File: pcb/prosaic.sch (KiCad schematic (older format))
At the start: 16 parts, among them J1 USB_C_Receptacle, SW1 SW_PUSH, U1 ATMEGA32U4, X1 XTAL_GND

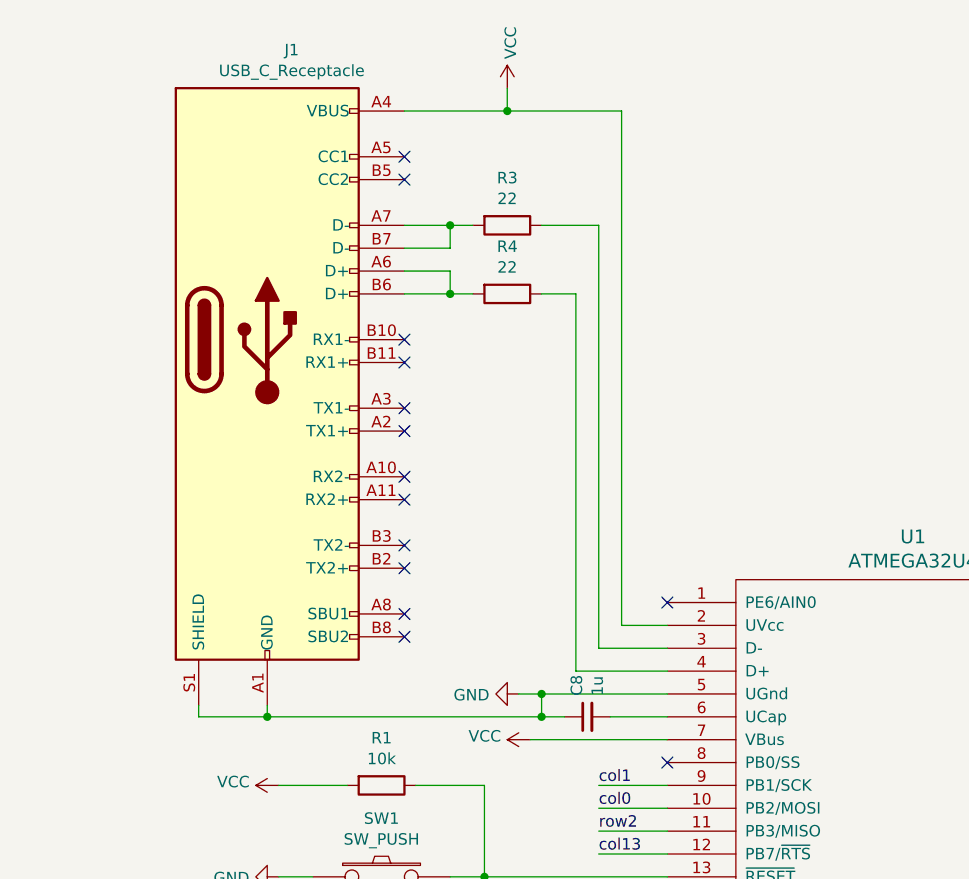
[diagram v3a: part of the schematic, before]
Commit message: Made trace change around crystal; updated case cad
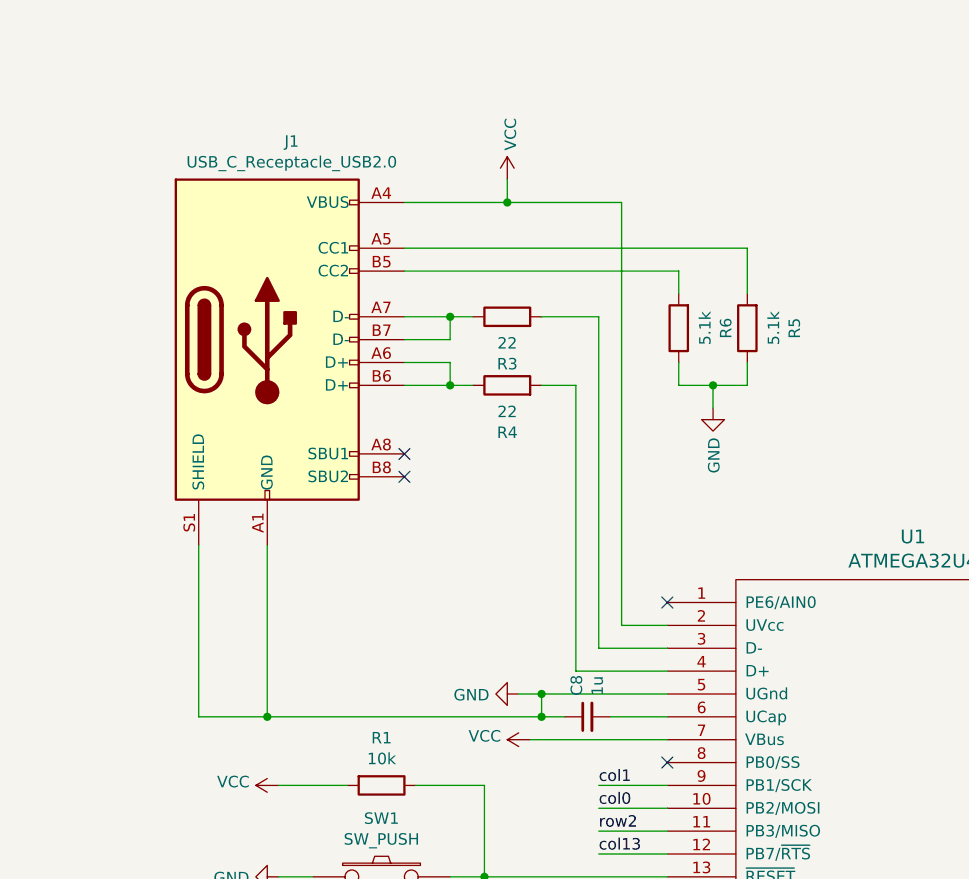
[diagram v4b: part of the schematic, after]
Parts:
- removed J1: USB_C_Receptacle, Connector_USB:USB_C_Receptacle_Amphenol_12401610E4-2A, symbol Connector:USB_C_Receptacle
- added J1: USB_C_Receptacle_USB2.0, Connector_USB:USB_C_Receptacle_GCT_USB4085, symbol Connector:USB_C_Receptacle_USB2.0
- added R5, R6: 5.1k, Resistor_SMD:R_0805_2012Metric_Pad1.15x1.40mm_HandSolder, symbol Device:R
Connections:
- net GND: now also J1.A1 (GND), J1.A12 (GND), J1.B1 (GND), J1.B12 (GND), J1.S1 (SHIELD), R5.1, R6.1
- net VCC: now also J1.A4 (VBUS), J1.A9 (VBUS), J1.B4 (VBUS), J1.B9 (VBUS)
- net at R4.1: now also J1.A6 (D+), J1.B6 (D+); no longer U1.4 (D+)
- net at R4.2: now also U1.4 (D+)
- net at R3.1: now also J1.A7 (D-), J1.B7 (D-); no longer U1.3 (D-)
- net at R3.2: now also U1.3 (D-)
- new net: J1.B5 (CC2), R6.2
- new net: J1.A5 (CC1), R5.2
- no-connect marks 16 -> 6
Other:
- moved on the sheet: R3, R4
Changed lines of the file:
@@
 Sheet 1 2
 Title "Prosaic"
-Date "2020-07-28"
-Rev "A"
+Date "2020-08-02"
+Rev "A.1"
 Comp ""
 Comment1 "by SiriusSam"
@@
 	6250 3850 6650 3850
 Wire Wire Line
-	6100 2200 6250 2200
+	6100 2600 6250 2600
 Wire Wire Line
 	6350 3750 6650 3750
 Wire Wire Line
-	6350 1900 6350 3750
-Wire Wire Line
-	5700 2100 5700 2200
-Wire Wire Line
-	5700 2000 5700 1900
+	5700 2500 5700 2600
+Wire Wire Line
+	5700 2400 5700 2300
 $Comp
 L Device:R R4
 U 1 1 5F1AE097
-P 5950 2200
-F 0 "R4" V 5743 2200 50  0000 C CNN
-F 1 "22" V 5834 2200 50  0000 C CNN
-F 2 "Resistor_SMD:R_0805_2012Metric_Pad1.15x1.40mm_HandSolder" V 5880 2200 50  0001 C CNN
-F 3 "~" H 5950 2200 50  0001 C CNN
-	1    5950 2200
-	0    1    1    0
+P 5950 2600
+F 0 "R4" V 5743 2600 50  0000 C CNN
+F 1 "22" V 5834 2600 50  0000 C CNN
+F 2 "Resistor_SMD:R_0805_2012Metric_Pad1.15x1.40mm_HandSolder" V 5880 2600 50  0001 C CNN
+F 3 "~" H 5950 2600 50  0001 C CNN
+	1    5950 2600
+	0    -1   -1   0
 $EndComp
 $Comp
 L Device:R R3
 U 1 1 5F1AE09D
-P 5950 1900
-F 0 "R3" V 5743 1900 50  0000 C CNN
-F 1 "22" V 5834 1900 50  0000 C CNN
-F 2 "Resistor_SMD:R_0805_2012Metric_Pad1.15x1.40mm_HandSolder" V 5880 1900 50  0001 C CNN
-F 3 "~" H 5950 1900 50  0001 C CNN
-	1    5950 1900
-	0    1    1    0
-$EndComp
-Connection ~ 5950 1400
-Wire Wire Line
-	6450 1400 5950 1400
-Wire Wire Line
-	6450 3650 6450 1400
+P 5950 2300
+F 0 "R3" V 5743 2300 50  0000 C CNN
+F 1 "22" V 5834 2300 50  0000 C CNN
+F 2 "Resistor_SMD:R_0805_2012Metric_Pad1.15x1.40mm_HandSolder" V 5880 2300 50  0001 C CNN
+F 3 "~" H 5950 2300 50  0001 C CNN
+	1    5950 2300
+	0    -1   -1   0
+$EndComp
+Connection ~ 5950 1800
+Wire Wire Line
+	6450 1800 5950 1800
 Wire Wire Line
 	6650 3650 6450 3650
 Wire Wire Line
-	5950 1300 5950 1400
+	5950 1700 5950 1800
 $Comp
 L power:VCC #PWR0110
 U 1 1 5F1AE0A9
-P 5950 1300
-F 0 "#PWR0110" H 5950 1150 50  0001 C CNN
-F 1 "VCC" V 5965 1427 50  0000 L CNN
-F 2 "" H 5950 1300 50  0001 C CNN
-F 3 "" H 5950 1300 50  0001 C CNN
-	1    5950 1300
+P 5950 1700
+F 0 "#PWR0110" H 5950 1550 50  0001 C CNN
+F 1 "VCC" V 5965 1827 50  0000 L CNN
+F 2 "" H 5950 1700 50  0001 C CNN
+F 3 "" H 5950 1700 50  0001 C CNN
+	1    5950 1700
 	1    0    0    -1
 $EndComp
@@
 NoConn ~ 8800 3750
 Wire Wire Line
-	6100 1900 6350 1900
-Wire Wire Line
-	6250 2200 6250 3850
-Connection ~ 5700 1900
-Connection ~ 5700 2200
-Wire Wire Line
-	5700 2200 5800 2200
-Wire Wire Line
-	5700 1900 5800 1900
-Wire Wire Line
-	4600 4000 4600 4050
-Wire Wire Line
-	5500 2000 5700 2000
-Wire Wire Line
-	5500 2200 5700 2200
-Wire Wire Line
-	5500 1900 5700 1900
-Wire Wire Line
-	5500 2100 5700 2100
-Wire Wire Line
-	5950 1400 5500 1400
-$Comp
-L Connector:USB_C_Receptacle J1
-U 1 1 5FF17B03
-P 4900 2400
-F 0 "J1" H 5007 3667 50  0000 C CNN
-F 1 "USB_C_Receptacle" H 5007 3576 50  0000 C CNN
-F 2 "Connector_USB:USB_C_Receptacle_Amphenol_12401610E4-2A" H 5050 2400 50  0001 C CNN
-F 3 "https://www.usb.org/sites/default/files/documents/usb_type-c.zip" H 5050 2400 50  0001 C CNN
-	1    4900 2400
-	1    0    0    -1
-$EndComp
-NoConn ~ 5500 1600
-NoConn ~ 5500 1700
-NoConn ~ 5500 2400
-NoConn ~ 5500 2500
-NoConn ~ 5500 2700
-NoConn ~ 5500 2800
-NoConn ~ 5500 3000
-NoConn ~ 5500 3100
-NoConn ~ 5500 3300
-NoConn ~ 5500 3400
-NoConn ~ 5500 3600
-NoConn ~ 5500 3700
+	6100 2300 6350 2300
+Connection ~ 5700 2300
+Connection ~ 5700 2600
+Wire Wire Line
+	5700 2600 5800 2600
+Wire Wire Line
+	5700 2300 5800 2300
+Wire Wire Line
+	5500 2400 5700 2400
+Wire Wire Line
+	5500 2600 5700 2600
+Wire Wire Line
+	5500 2300 5700 2300
+Wire Wire Line
+	5500 2500 5700 2500
+Wire Wire Line
+	5950 1800 5500 1800
 $Sheet
 S 1750 3750 1500 1700
@@
 Wire Wire Line
 	8800 5550 9000 5550
-Wire Wire Line
-	4600 4050 4900 4050
-Wire Wire Line
-	4900 4000 4900 4050
-Connection ~ 4900 4050
-Wire Wire Line
-	4900 4050 6100 4050
 Text Label 1500 4900 0    50   ~ 0
 col2
@@
 Wire Wire Line
 	6350 4650 6650 4650
+$Comp
+L Device:R R6
+U 1 1 5F27B3AB
+P 6700 2350
+F 0 "R6" V 6493 2350 50  0000 C CNN
+F 1 "5.1k" V 6584 2350 50  0000 C CNN
+F 2 "Resistor_SMD:R_0805_2012Metric_Pad1.15x1.40mm_HandSolder" V 6630 2350 50  0001 C CNN
+F 3 "~" H 6700 2350 50  0001 C CNN
+	1    6700 2350
+	-1   0    0    1
+$EndComp
+$Comp
+L Device:R R5
+U 1 1 5F27BA1B
+P 7000 2350
+F 0 "R5" V 6793 2350 50  0000 C CNN
+F 1 "5.1k" V 6884 2350 50  0000 C CNN
+F 2 "Resistor_SMD:R_0805_2012Metric_Pad1.15x1.40mm_HandSolder" V 6930 2350 50  0001 C CNN
+F 3 "~" H 7000 2350 50  0001 C CNN
+	1    7000 2350
+	-1   0    0    1
+$EndComp
+Wire Wire Line
+	5500 2000 7000 2000
+Wire Wire Line
+	7000 2000 7000 2200
+Wire Wire Line
+	6700 2200 6700 2100
+Wire Wire Line
+	6700 2100 5500 2100
+$Comp
+L power:GND #PWR0118
+U 1 1 5F2A63DE
+P 6850 2700
+F 0 "#PWR0118" H 6850 2450 50  0001 C CNN
+F 1 "GND" V 6855 2572 50  0000 R CNN
+F 2 "" H 6850 2700 50  0001 C CNN
+F 3 "" H 6850 2700 50  0001 C CNN
+	1    6850 2700
+	1    0    0    -1
+$EndComp
+Wire Wire Line
+	6700 2500 6700 2600
+Wire Wire Line
+	6700 2600 6850 2600
+Wire Wire Line
+	6850 2600 6850 2700
+Wire Wire Line
+	7000 2500 7000 2600
+Wire Wire Line
+	7000 2600 6850 2600
+Connection ~ 6850 2600
+$Comp
+L Connector:USB_C_Receptacle_USB2.0 J1
+U 1 1 5F2C13EB
+P 4900 2400
+F 0 "J1" H 5007 3267 50  0000 C CNN
+F 1 "USB_C_Receptacle_USB2.0" H 5007 3176 50  0000 C CNN
+F 2 "Connector_USB:USB_C_Receptacle_GCT_USB4085" H 5050 2400 50  0001 C CNN
+F 3 "https://www.usb.org/sites/default/files/documents/usb_type-c.zip" H 5050 2400 50  0001 C CNN
+	1    4900 2400
+	1    0    0    -1
+$EndComp
+NoConn ~ 5500 2900
+NoConn ~ 5500 3000
+Wire Wire Line
+	4600 4050 4900 4050
+Wire Wire Line
+	4600 3300 4600 4050
+Wire Wire Line
+	4900 3300 4900 4050
+Connection ~ 4900 4050
+Wire Wire Line
+	4900 4050 6100 4050
+Wire Wire Line
+	6250 2600 6250 3850
+Wire Wire Line
+	6350 2300 6350 3750
+Wire Wire Line
+	6450 3650 6450 1800
 $EndSCHEMATC
